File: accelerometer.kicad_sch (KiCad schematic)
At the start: 3 parts, among them U7 kx13x

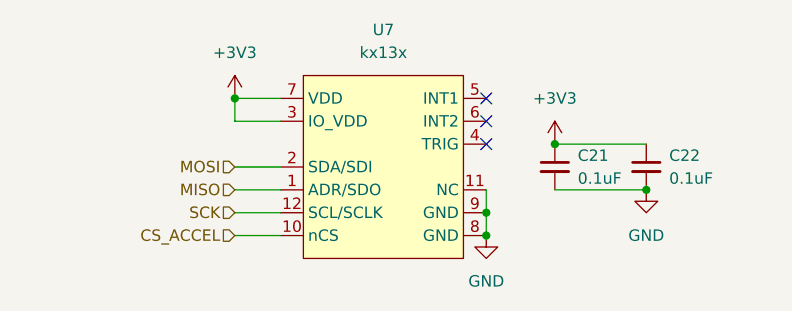
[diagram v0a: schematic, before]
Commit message: Connected topsheet
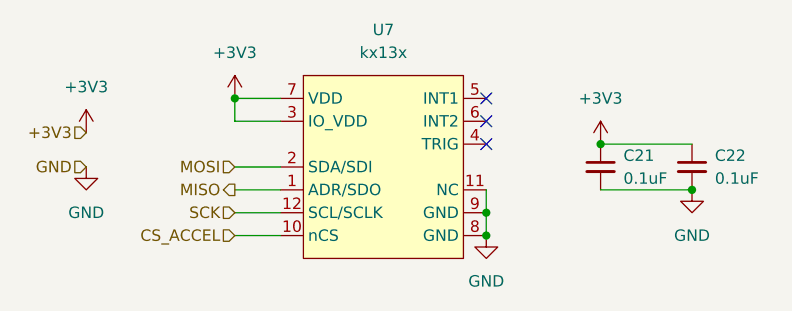
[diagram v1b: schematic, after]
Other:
- moved on the sheet: C21, C22
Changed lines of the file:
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@@
 	)
 	(junction
-		(at 128.27 69.85)
+		(at 133.35 69.85)
 		(diameter 0)
 		(color 0 0 0 0)
@@
 	)
 	(junction
-		(at 118.11 64.77)
+		(at 123.19 64.77)
 		(diameter 0)
 		(color 0 0 0 0)
@@
 	(wire
 		(pts
-			(xy 128.27 69.85) (xy 118.11 69.85)
+			(xy 133.35 69.85) (xy 123.19 69.85)
 		)
 		(stroke
@@
 	(wire
 		(pts
-			(xy 118.11 64.77) (xy 128.27 64.77)
+			(xy 123.19 64.77) (xy 133.35 64.77)
 		)
 		(stroke
@@
 	)
 	(hierarchical_label "MISO"
-		(shape input)
+		(shape output)
 		(at 82.55 69.85 180)
 		(effects
@@
 		)
 	)
+	(hierarchical_label "GND"
+		(shape input)
+		(at 66.04 67.31 180)
+		(effects
+			(font
+				(size 1.27 1.27)
+			)
+			(justify right)
+		)
+	)
+	(hierarchical_label "+3V3"
+		(shape input)
+		(at 66.04 63.5 180)
+		(effects
+			(font
+				(size 1.27 1.27)
+			)
+			(justify right)
+		)
+	)
 	(symbol
 		(lib_id "power:GND")
-		(at 128.27 69.85 0)
+		(at 133.35 69.85 0)
 		(unit 1)
 		(exclude_from_sim no)
@@
 		(fields_autoplaced yes)
 		(property "Reference" "#PWR078"
-			(at 128.27 76.2 0)
+			(at 133.35 76.2 0)
 			(effects
 				(font
@@
 		)
 		(property "Value" "GND"
-			(at 128.27 74.93 0)
+			(at 133.35 74.93 0)
 			(effects
 				(font
@@
 		)
 		(property "Footprint" ""
-			(at 128.27 69.85 0)
+			(at 133.35 69.85 0)
 			(effects
 				(font
@@
 		)
 		(property "Datasheet" ""
-			(at 128.27 69.85 0)
+			(at 133.35 69.85 0)
 			(effects
 				(font
@@
 		)
 		(property "Description" "Power symbol creates a global label with name \"GND\" , ground"
-			(at 128.27 69.85 0)
+			(at 133.35 69.85 0)
 			(effects
 				(font
@@
 	(symbol
 		(lib_id "power:+3V3")
-		(at 118.11 64.77 0)
+		(at 123.19 64.77 0)
 		(unit 1)
 		(exclude_from_sim no)
@@
 		(fields_autoplaced yes)
 		(property "Reference" "#PWR077"
-			(at 118.11 68.58 0)
+			(at 123.19 68.58 0)
 			(effects
 				(font
@@
 		)
 		(property "Value" "+3V3"
-			(at 118.11 59.69 0)
+			(at 123.19 59.69 0)
 			(effects
 				(font
@@
 		)
 		(property "Footprint" ""
-			(at 118.11 64.77 0)
+			(at 123.19 64.77 0)
 			(effects
 				(font
@@
 		)
 		(property "Datasheet" ""
-			(at 118.11 64.77 0)
+			(at 123.19 64.77 0)
 			(effects
 				(font
@@
 		)
 		(property "Description" "Power symbol creates a global label with name \"+3V3\""
-			(at 118.11 64.77 0)
+			(at 123.19 64.77 0)
 			(effects
 				(font
@@
 	(symbol
 		(lib_id "Device:C_Small")
-		(at 118.11 67.31 0)
+		(at 123.19 67.31 0)
 		(unit 1)
 		(exclude_from_sim no)
@@
 		(fields_autoplaced yes)
 		(property "Reference" "C21"
-			(at 120.65 66.0462 0)
+			(at 125.73 66.0462 0)
 			(effects
 				(font
@@
 		)
 		(property "Value" "0.1uF"
-			(at 120.65 68.5862 0)
+			(at 125.73 68.5862 0)
 			(effects
 				(font
@@
 		)
 		(property "Footprint" ""
-			(at 118.11 67.31 0)
+			(at 123.19 67.31 0)
 			(effects
 				(font
@@
 		)
 		(property "Datasheet" "~"
-			(at 118.11 67.31 0)
+			(at 123.19 67.31 0)
 			(effects
 				(font
@@
 		)
 		(property "Description" "Unpolarized capacitor, small symbol"
-			(at 118.11 67.31 0)
+			(at 123.19 67.31 0)
 			(effects
 				(font
@@
 	(symbol
 		(lib_id "Device:C_Small")
-		(at 128.27 67.31 0)
+		(at 133.35 67.31 0)
 		(unit 1)
 		(exclude_from_sim no)
@@
 		(fields_autoplaced yes)
 		(property "Reference" "C22"
-			(at 130.81 66.0462 0)
+			(at 135.89 66.0462 0)
 			(effects
 				(font
@@
 		)
 		(property "Value" "0.1uF"
-			(at 130.81 68.5862 0)
+			(at 135.89 68.5862 0)
 			(effects
 				(font
@@
 		)
 		(property "Footprint" ""
-			(at 128.27 67.31 0)
+			(at 133.35 67.31 0)
 			(effects
 				(font
@@
 		)
 		(property "Datasheet" "~"
-			(at 128.27 67.31 0)
+			(at 133.35 67.31 0)
 			(effects
 				(font
@@
 		)
 		(property "Description" "Unpolarized capacitor, small symbol"
-			(at 128.27 67.31 0)
+			(at 133.35 67.31 0)
 			(effects
 				(font
@@
 					(unit 1)
 				)
+			)
+		)
+	)
+	(symbol
+		(lib_id "power:GND")
+		(at 66.04 67.31 0)
+		(unit 1)
+		(exclude_from_sim no)
+		(in_bom yes)
+		(on_board yes)
+		(dnp no)
+		(fields_autoplaced yes)
+		(property "Reference" "#PWR080"
+			(at 66.04 73.66 0)
+			(effects
+				(font
+					(size 1.27 1.27)
+				)
+				(hide yes)
+			)
+		)
+		(property "Value" "GND"
+			(at 66.04 72.39 0)
+			(effects
+				(font
+					(size 1.27 1.27)
+				)
+			)
+		)
+		(property "Footprint" ""
+			(at 66.04 67.31 0)
+			(effects
+				(font
+					(size 1.27 1.27)
+				)
+				(hide yes)
+			)
+		)
+		(property "Datasheet" ""
+			(at 66.04 67.31 0)
+			(effects
+				(font
+					(size 1.27 1.27)
+				)
+				(hide yes)
+			)
+		)
+		(property "Description" "Power symbol creates a global label with name \"GND\" , ground"
+			(at 66.04 67.31 0)
+			(effects
+				(font
+					(size 1.27 1.27)
+				)
+				(hide yes)
+			)
+		)
+		(pin "1"
+		)
+		(instances
+			(project "Blaze-NT"
+				(path "/2c2eadf0-5503-4531-8753-1a232087fe8c/b9b0c40a-7771-4bc1-adbf-abe0201c34d0/9a6553ac-59f7-4d16-afa0-9743f2c46ffa"
+					(reference "#PWR080")
+					(unit 1)
+				)
+			)
+		)
+	)
+	(symbol
+		(lib_id "power:+3V3")
+		(at 66.04 63.5 0)
+		(unit 1)
+		(exclude_from_sim no)
+		(in_bom yes)
+		(on_board yes)
+		(dnp no)
+		(fields_autoplaced yes)
+		(property "Reference" "#PWR081"
+			(at 66.04 67.31 0)
+			(effects
+				(font
+					(size 1.27 1.27)
+				)
+				(hide yes)
+			)
+		)
+		(property "Value" "+3V3"
+			(at 66.04 58.42 0)
+			(effects
+				(font
+					(size 1.27 1.27)
+				)
+			)
+		)
+		(property "Footprint" ""
+			(at 66.04 63.5 0)
+			(effects
+				(font
+					(size 1.27 1.27)
+				)
+				(hide yes)
+			)
+		)
+		(property "Datasheet" ""
+			(at 66.04 63.5 0)
+			(effects
+				(font
+					(size 1.27 1.27)
+				)
+				(hide yes)
+			)
+		)
+		(property "Description" "Power symbol creates a global label with name \"+3V3\""
+			(at 66.04 63.5 0)
+			(effects
+				(font
+					(size 1.27 1.27)
+				)
+				(hide yes)
+			)
+		)
+		(pin "1"
+		)
+		(instances
+			(project "Blaze-NT"
+				(path "/2c2eadf0-5503-4531-8753-1a232087fe8c/b9b0c40a-7771-4bc1-adbf-abe0201c34d0/9a6553ac-59f7-4d16-afa0-9743f2c46ffa"
+					(reference "#PWR081")
+					(unit 1)
+				)

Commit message: Footprint selection
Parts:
- C21, C22: footprint (none) -> Capacitor_SMD:C_0603_1608Metric
- U7: footprint (none) -> Package_SO:VSSOP-10_3x3mm_P0.5mm
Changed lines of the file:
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@@
 			)
 		)
-		(property "Footprint" ""
+		(property "Footprint" "Capacitor_SMD:C_0603_1608Metric"
 			(at 123.19 67.31 0)
 			(effects
@@
 			)
 		)
-		(property "Footprint" ""
+		(property "Footprint" "Capacitor_SMD:C_0603_1608Metric"
 			(at 133.35 67.31 0)
 			(effects
@@
 			)
 		)
-		(property "Footprint" ""
+		(property "Footprint" "Package_SO:VSSOP-10_3x3mm_P0.5mm"
 			(at 77.47 53.34 0)
 			(effects

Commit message: Radio footprint selection
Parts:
- renumbered C21 to C23, C22 to C24, U7 to U8
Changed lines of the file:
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@@
 		(dnp no)
 		(fields_autoplaced yes)
-		(property "Reference" "#PWR079"
+		(property "Reference" "#PWR085"
 			(at 133.35 76.2 0)
 			(effects
@@
 			(project "Blaze-NT"
 				(path "/2c2eadf0-5503-4531-8753-1a232087fe8c/b9b0c40a-7771-4bc1-adbf-abe0201c34d0/9a6553ac-59f7-4d16-afa0-9743f2c46ffa"
-					(reference "#PWR079")
+					(reference "#PWR085")
 					(unit 1)
 				)
@@
 		(dnp no)
 		(fields_autoplaced yes)
-		(property "Reference" "#PWR077"
+		(property "Reference" "#PWR083"
 			(at 123.19 68.58 0)
 			(effects
@@
 			(project "Blaze-NT"
 				(path "/2c2eadf0-5503-4531-8753-1a232087fe8c/b9b0c40a-7771-4bc1-adbf-abe0201c34d0/9a6553ac-59f7-4d16-afa0-9743f2c46ffa"
-					(reference "#PWR077")
+					(reference "#PWR083")
 					(unit 1)
 				)
@@
 		(dnp no)
 		(fields_autoplaced yes)
-		(property "Reference" "C21"
+		(property "Reference" "C23"
 			(at 125.73 66.0462 0)
 			(effects
@@
 			(project ""
 				(path "/2c2eadf0-5503-4531-8753-1a232087fe8c/b9b0c40a-7771-4bc1-adbf-abe0201c34d0/9a6553ac-59f7-4d16-afa0-9743f2c46ffa"
-					(reference "C21")
+					(reference "C23")
 					(unit 1)
 				)
@@
 		(dnp no)
 		(fields_autoplaced yes)
-		(property "Reference" "#PWR075"
+		(property "Reference" "#PWR081"
 			(at 82.55 63.5 0)
 			(effects
@@
 			(project ""
 				(path "/2c2eadf0-5503-4531-8753-1a232087fe8c/b9b0c40a-7771-4bc1-adbf-abe0201c34d0/9a6553ac-59f7-4d16-afa0-9743f2c46ffa"
-					(reference "#PWR075")
+					(reference "#PWR081")
 					(unit 1)
 				)
@@
 		(dnp no)
 		(fields_autoplaced yes)
-		(property "Reference" "C22"
+		(property "Reference" "C24"
 			(at 135.89 66.0462 0)
 			(effects
@@
 			(project "Blaze-NT"
 				(path "/2c2eadf0-5503-4531-8753-1a232087fe8c/b9b0c40a-7771-4bc1-adbf-abe0201c34d0/9a6553ac-59f7-4d16-afa0-9743f2c46ffa"
-					(reference "C22")
+					(reference "C24")
 					(unit 1)
 				)
@@
 		(dnp no)
 		(fields_autoplaced yes)
-		(property "Reference" "#PWR078"
+		(property "Reference" "#PWR084"
 			(at 66.04 73.66 0)
 			(effects
@@
 			(project "Blaze-NT"
 				(path "/2c2eadf0-5503-4531-8753-1a232087fe8c/b9b0c40a-7771-4bc1-adbf-abe0201c34d0/9a6553ac-59f7-4d16-afa0-9743f2c46ffa"
-					(reference "#PWR078")
+					(reference "#PWR084")
 					(unit 1)
 				)
@@
 		(dnp no)
 		(fields_autoplaced yes)
-		(property "Reference" "#PWR076"
+		(property "Reference" "#PWR082"
 			(at 66.04 67.31 0)
 			(effects
@@
 			(project "Blaze-NT"
 				(path "/2c2eadf0-5503-4531-8753-1a232087fe8c/b9b0c40a-7771-4bc1-adbf-abe0201c34d0/9a6553ac-59f7-4d16-afa0-9743f2c46ffa"
-					(reference "#PWR076")
+					(reference "#PWR082")
 					(unit 1)
 				)
@@
 		(dnp no)
 		(fields_autoplaced yes)
-		(property "Reference" "U7"
+		(property "Reference" "U8"
 			(at 99.06 52.07 0)
 			(effects
@@
 			(project ""
 				(path "/2c2eadf0-5503-4531-8753-1a232087fe8c/b9b0c40a-7771-4bc1-adbf-abe0201c34d0/9a6553ac-59f7-4d16-afa0-9743f2c46ffa"
-					(reference "U7")
+					(reference "U8")
 					(unit 1)
 				)
@@
 		(dnp no)
 		(fields_autoplaced yes)
-		(property "Reference" "#PWR080"
+		(property "Reference" "#PWR086"
 			(at 110.49 81.28 0)
 			(effects
@@
 			(project "Blaze-NT"
 				(path "/2c2eadf0-5503-4531-8753-1a232087fe8c/b9b0c40a-7771-4bc1-adbf-abe0201c34d0/9a6553ac-59f7-4d16-afa0-9743f2c46ffa"
-					(reference "#PWR080")
-					(unit 1)
-				)
+					(reference "#PWR086")
+					(unit 1)
+				)

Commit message: PCB work
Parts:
- U8: footprint Package_SO:VSSOP-10_3x3mm_P0.5mm -> Avionics_Feet:XDCR_KX003-1077
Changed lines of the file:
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@@
 			)
 		)
-		(property "Footprint" "Package_SO:VSSOP-10_3x3mm_P0.5mm"
+		(property "Footprint" "Avionics_Feet:XDCR_KX003-1077"
 			(at 77.47 53.34 0)
 			(effects

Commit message: Addeed part numbers
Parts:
- C23, C24: LCSC (none) -> C14663
- U8: LCSC (none) -> C2157908
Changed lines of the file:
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@@
+			)
+		)
+		(property "LCSC" "C14663"
+			(at 123.19 67.31 0)
+			(effects
+				(font
+					(size 1.27 1.27)
+				)
+				(hide yes)
 			)
 		)
@@
 			)
 		)
+		(property "LCSC" "C14663"
+			(at 133.35 67.31 0)
+			(effects
+				(font
+					(size 1.27 1.27)
+				)
+				(hide yes)
+			)
+		)
 		(pin "1"
 		)
@@
 			(effects
 				(font
+					(size 1.27 1.27)
+				)
+				(hide yes)
+			)
+		)
+		(property "LCSC" "C2157908"
+			(at 99.06 66.04 0)
+			(effects
+				(font

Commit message: Added Digikey Components
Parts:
- U8: Digikey (none) -> KX134-1211
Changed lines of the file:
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@@
+			)
+		)
+		(property "Digikey" ""
+			(at 123.19 67.31 0)
+			(effects
+				(font
+					(size 1.27 1.27)
+				)
+				(hide yes)
 			)
 		)
@@
 			)
 		)
+		(property "Digikey" ""
+			(at 133.35 67.31 0)
+			(effects
+				(font
+					(size 1.27 1.27)
+				)
+				(hide yes)
+			)
+		)
 		(pin "1"
 		)
@@
 			(at 99.06 66.04 0)
 			(effects
+				(font
+					(size 1.27 1.27)
+				)
+				(hide yes)
+			)
+		)
+		(property "Digikey" "KX134-1211"
+			(at 99.06 66.04 0)
+			(effects
